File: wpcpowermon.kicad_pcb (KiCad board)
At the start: 2 copper layers, 12 parts, among them J1 Screw_Terminal_01x02, J1001 Conn_02x17_Odd_Even, U3 74HC245, U4 74HC245, U6 MAX485E

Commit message: Version 0.1
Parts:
- added ?: MountingHole_3mm, MountingHole:MountingHole_3mm, F.Cu at (151.4, 66.0)
- added ?: MountingHole_3mm, MountingHole:MountingHole_3mm, F.Cu at (84.8, 123.4)
- added ?: MountingHole_3mm, MountingHole:MountingHole_3mm, F.Cu at (151.4, 123.4)
- added ?: MountingHole_3mm, MountingHole:MountingHole_3mm, F.Cu at (84.8, 66.0)
- added J2: LED, Connector_Molex:Molex_SL_171971-0004_1x04_P2.54mm_Vertical, F.Cu at (143.3, 67.3)
- added J3: LED, Connector_Molex:Molex_SL_171971-0004_1x04_P2.54mm_Vertical, F.Cu at (143.3, 81.8)
- added J4: Screw_Terminal_01x02, TerminalBlock_4Ucon:TerminalBlock_4Ucon_1x02_P3.50mm_Horizontal, F.Cu at (143.9, 103.4)
- added U5: Pico, MCU_RaspberryPi_and_Boards:RPi_Pico_SMD_TH, F.Cu at (121.9, 89.9)
- J1: value Screw_Terminal_01x02 -> Screw_Terminal_01x04; footprint TerminalBlock_4Ucon:TerminalBlock_4Ucon_1x02_P3.50mm_Horizontal -> TerminalBlock_4Ucon:TerminalBlock_4Ucon_1x04_P3.50mm_Horizontal
- moved J1 83.2 mm to (116.7, 122.3)
- moved R2 63.6 mm to (141.7, 99.1), turned to 180 degrees
- moved U6 55.6 mm to (137.4, 112.0)
- moved R1 52.8 mm to (144.3, 124.5), turned to 180 degrees
- moved JP1 37.7 mm to (132.8, 124.5), turned to 90 degrees
- moved C3 32.8 mm to (148.8, 113.0), turned to -90 degrees
- moved D1 24.3 mm to (140.5, 95.0), turned to 180 degrees
- moved C1 0.89 mm to (99.7, 64.5)
- moved U4 0.51 mm to (97.2, 68.1)
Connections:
- C3 pad 1: +3V3 -> +5V
- D1 pad 2: (no net) -> Net-(D1-Pad2)
- J1 pad 1: Net-(J1-Pad1) -> +5V
- J1 pad 2: Net-(J1-Pad2) -> Net-(R1-Pad1)
- J1001 pad 1: (no net) -> unconnected-(J1001-Pad1)
- J1001 pad 2: (no net) -> unconnected-(J1001-Pad2)
- J1001 pad 3: (no net) -> unconnected-(J1001-Pad3)
- J1001 pad 31: (no net) -> unconnected-(J1001-Pad31)
- J1001 pad 32: (no net) -> unconnected-(J1001-Pad32)
- J1001 pad 33: (no net) -> unconnected-(J1001-Pad33)
- J1001 pad 4: (no net) -> unconnected-(J1001-Pad4)
- J1001 pad 5: (no net) -> unconnected-(J1001-Pad5)
- J1001 pad 6: (no net) -> unconnected-(J1001-Pad6)
- JP1 pad 1: Net-(J1-Pad2) -> Net-(JP1-Pad1)
- R1 pad 1: Net-(J1-Pad1) -> Net-(R1-Pad1)
- U3 pad 11: (no net) -> //ZEROCROSS
- U3 pad 12: (no net) -> //LAMP ROW
- U3 pad 13: (no net) -> //LAMP COL
- U3 pad 14: (no net) -> //SOL2
- U3 pad 15: (no net) -> //SOL4
- U3 pad 16: (no net) -> //SOL3
- U3 pad 17: (no net) -> //SOL1
- U3 pad 18: (no net) -> //TRIACS
- U4 pad 11: (no net) -> /D7
- U4 pad 12: (no net) -> /D6
- U4 pad 13: (no net) -> /D5
- U4 pad 14: (no net) -> /D4
- U4 pad 15: (no net) -> /D3
- U4 pad 16: (no net) -> /D2
- U4 pad 17: (no net) -> /D1
- U4 pad 18: (no net) -> /D0
- U6 pad 1: (no net) -> Net-(U5-Pad22)
- U6 pad 4: (no net) -> Net-(U5-Pad21)
- U6 pad 5: (no net) -> GND
- U6 pad 6: Net-(J1-Pad1) -> Net-(R1-Pad1)
- U6 pad 7: Net-(J1-Pad2) -> Net-(JP1-Pad1)
- U6 pad 8: (no net) -> +5V
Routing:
- net +5V: track 0.00 -> 118.7 mm
- net Net-(R1-Pad1): track 0.00 -> 34.3 mm
- net Net-(JP1-Pad1): track 0.00 -> 28.4 mm
- net Net-(J2-Pad3): track 0.00 -> 23.1 mm
- net Net-(J3-Pad3): track 0.00 -> 21.9 mm
- net Net-(J3-Pad2): track 0.00 -> 21.6 mm
- net Net-(J2-Pad2): track 0.00 -> 20.3 mm
- net //SOL3: track 0.00 -> 17.8 mm
- net //SOL4: track 0.00 -> 17.3 mm
- net //SOL2: track 0.00 -> 17.0 mm
- net //SOL1: track 0.00 -> 17.0 mm
- net //TRIACS: track 0.00 -> 16.8 mm
- net Net-(U5-Pad24): track 0.00 -> 15.3 mm
- net //LAMP COL: track 0.00 -> 14.5 mm
- net //LAMP ROW: track 0.00 -> 14.3 mm
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- added copper zone on F.Cu, net +3V3
- added copper zone on B.Cu, net GND
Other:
- board outline added: 75.2 x 66.5 mm
- board text added: "+ A B -"
- board text added: "1"
- board text added: "TERM"
- board text added: "WPC PowerMON 0.1 (c) 2021 pinball-power.com"

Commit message: v 0.2
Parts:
- removed ? (x4): MountingHole_3mm, MountingHole:MountingHole_3mm
- removed J2: LED, Connector_Molex:Molex_SL_171971-0004_1x04_P2.54mm_Vertical
- removed U6: MAX485E, Package_DIP:DIP-8_W7.62mm_LongPads
- added J10: IO5, Connector_Molex:Molex_KK-254_AE-6410-03A_1x03_P2.54mm_Vertical, F.Cu at (154.3, 102.2)
- added J11: IO7, Connector_Molex:Molex_KK-254_AE-6410-03A_1x03_P2.54mm_Vertical, F.Cu at (154.3, 118.7)
- added J12: RS485, TerminalBlock_4Ucon:TerminalBlock_4Ucon_1x04_P3.50mm_Horizontal, F.Cu at (163.6, 81.9)
- added J5: IO4+3, Connector_Molex:Molex_KK-254_AE-6410-04A_1x04_P2.54mm_Vertical, F.Cu at (144.2, 88.3)
- added J6: IO6+5, Connector_Molex:Molex_KK-254_AE-6410-04A_1x04_P2.54mm_Vertical, F.Cu at (144.2, 104.8)
- added J7: IO8+7, Connector_Molex:Molex_KK-254_AE-6410-04A_1x04_P2.54mm_Vertical, F.Cu at (144.2, 121.3)
- added J8: IO1, Connector_Molex:Molex_KK-254_AE-6410-03A_1x03_P2.54mm_Vertical, F.Cu at (154.3, 69.2)
- added J9: IO3, Connector_Molex:Molex_KK-254_AE-6410-03A_1x03_P2.54mm_Vertical, F.Cu at (154.3, 85.7)
- added JP2: 5V, Connector_PinHeader_2.54mm:PinHeader_1x02_P2.54mm_Vertical, F.Cu at (155.6, 123.2)
- added JP3: 5V, Connector_PinHeader_2.54mm:PinHeader_1x02_P2.54mm_Vertical, F.Cu at (142.9, 125.7)
- added JP4: 5V, Connector_PinHeader_2.54mm:PinHeader_1x02_P2.54mm_Vertical, F.Cu at (155.6, 106.7)
- added JP5: 5V, Connector_PinHeader_2.54mm:PinHeader_1x02_P2.54mm_Vertical, F.Cu at (142.9, 109.2)
- added JP6: 5V, Connector_PinHeader_2.54mm:PinHeader_1x02_P2.54mm_Vertical, F.Cu at (154.9, 90.2)
- added JP7: 5V, Connector_PinHeader_2.54mm:PinHeader_1x02_P2.54mm_Vertical, F.Cu at (142.9, 92.7)
- added JP8: 5V, Connector_PinHeader_2.54mm:PinHeader_1x02_P2.54mm_Vertical, F.Cu at (155.6, 73.7)
- added JP9: 5V, Connector_PinHeader_2.54mm:PinHeader_1x02_P2.54mm_Vertical, F.Cu at (142.9, 76.2)
- added REF**: MountingHole_4.3mm_M4, MountingHole:MountingHole_4.3mm_M4, F.Cu at (84.8, 66.0)
- added REF**: MountingHole_4.3mm_M4, MountingHole:MountingHole_4.3mm_M4, F.Cu at (174.2, 66.0)
- added REF**: MountingHole_4.3mm_M4, MountingHole:MountingHole_4.3mm_M4, F.Cu at (174.2, 123.4)
- added REF**: MountingHole_4.3mm_M4, MountingHole:MountingHole_4.3mm_M4, F.Cu at (84.8, 123.4)
- added REF**: OSHW-Logo2_14.6x12mm_SilkScreen, Symbol:OSHW-Logo2_14.6x12mm_SilkScreen, F.Cu at (122.2, 104.4)
- added U1: MAX485E, Package_DIP:DIP-8_W7.62mm_LongPads, F.Cu at (163.8, 94.3)
- J1: value Screw_Terminal_01x04 -> RS232; footprint TerminalBlock_4Ucon:TerminalBlock_4Ucon_1x04_P3.50mm_Horizontal -> Connector_Molex:Molex_KK-254_AE-6410-04A_1x04_P2.54mm_Vertical
- J1001: value Conn_02x17_Odd_Even -> WPC Bus
- J3: value LED -> IO2+1; footprint Connector_Molex:Molex_SL_171971-0004_1x04_P2.54mm_Vertical -> Connector_Molex:Molex_KK-254_AE-6410-04A_1x04_P2.54mm_Vertical
- J4: value Screw_Terminal_01x02 -> 5V
- JP1: value Jumper -> TERM
- moved J1 56.2 mm to (171.4, 109.5), turned to 180 degrees
- moved R1 55.1 mm to (170.4, 75.9), turned to 0 degrees
- moved JP1 52.1 mm to (170.9, 88.9)
- moved J4 31.6 mm to (118.7, 122.6), turned to 180 degrees
- moved C3 31.0 mm to (175.2, 96.8)
- moved R2 30.9 mm to (125.1, 125.1), turned to 0 degrees
- moved D1 28.7 mm to (127.6, 120.7)
- moved J3 10.1 mm to (144.2, 71.8), turned to 90 degrees
- moved J1001 1.55 mm to (86.1, 115.3)
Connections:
- D1 pad 2: Net-(D1-Pad2) -> +5V
- J1 pad 1: +5V -> GND
- J1 pad 2: Net-(R1-Pad1) -> /io/TX
- J1 pad 3: Net-(JP1-Pad1) -> /io/RX
- J1 pad 4: GND -> +5V
- J3 pad 1: +5V -> GND
- J3 pad 2: Net-(J3-Pad2) -> /io/IO2
- J3 pad 4: GND -> /io/IO1
- JP1 pad 1: Net-(JP1-Pad1) -> Net-(J12-Pad3)
- R1 pad 1: Net-(R1-Pad1) -> Net-(J12-Pad2)
- U5 pad 21: Net-(U5-Pad21) -> /io/TX
- U5 pad 22: Net-(U5-Pad22) -> /io/RX
- U5 pad 24: Net-(U5-Pad24) -> /io/IO8
- U5 pad 25: Net-(D1-Pad2) -> /io/IO7
- U5 pad 26: Net-(J3-Pad3) -> /io/IO6
- U5 pad 27: Net-(J3-Pad2) -> /io/IO5
- U5 pad 29: unconnected-(U5-Pad29) -> /io/IO4
- U5 pad 31: unconnected-(U5-Pad31) -> /io/IO3
- U5 pad 32: Net-(J2-Pad3) -> /io/IO2
- U5 pad 34: Net-(J2-Pad2) -> /io/IO1
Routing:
- net +5V: track 118.7 -> 197.6 mm
- net /io/TX: track 0.00 -> 60.8 mm
- net /io/RX: track 0.00 -> 59.7 mm
- net /io/IO8: track 0.00 -> 55.8 mm
- net +3V3: track 11.2 -> 64.9 mm
- net /io/IO1: track 0.00 -> 37.2 mm
- net Net-(R1-Pad1): track 34.3 -> 0.00 mm
- net /io/IO3: track 0.00 -> 30.0 mm
- net /io/IO7: track 0.00 -> 28.6 mm
- net Net-(JP1-Pad1): track 28.4 -> 0.00 mm
- net /io/IO2: track 0.00 -> 27.9 mm
- net Net-(J12-Pad2): track 0.00 -> 26.5 mm
- net /io/IO5: track 0.00 -> 25.3 mm
- net Net-(J2-Pad3): track 23.1 -> 0.00 mm
- net Net-(J3-Pad2): track 21.6 -> 0.00 mm
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- added copper zone on F.Cu, net +5V
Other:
- board size 75.2 x 66.5 mm -> 98.6 x 66.6 mm
- board text added: "WPC PowerMON v 0.2 (c) 2021 pinball-power.com"
- board text removed: "+ A B -"
- board text removed: "TERM"
- board text removed: "WPC PowerMON 0.1 (c) 2021 pinball-power.com"

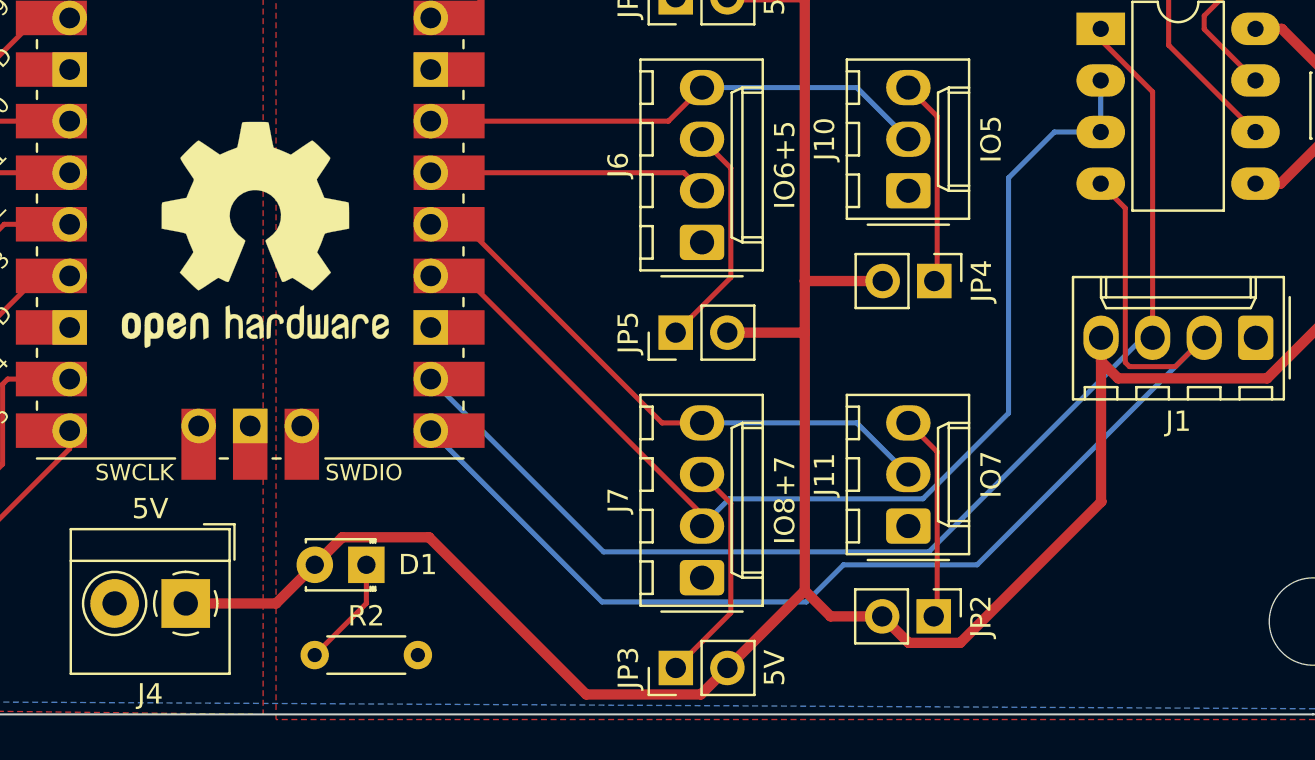
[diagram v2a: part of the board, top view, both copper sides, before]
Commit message: Added OHC logo
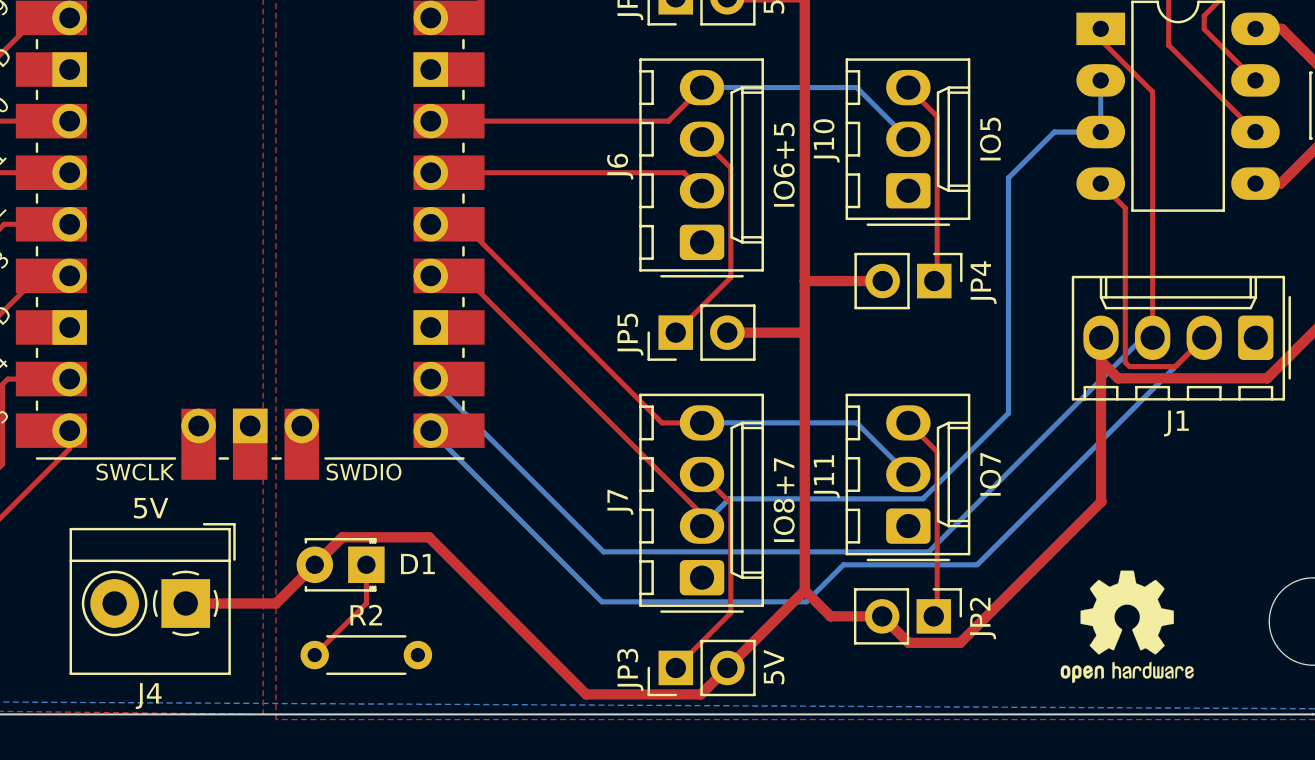
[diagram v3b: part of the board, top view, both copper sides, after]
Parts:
- removed the REF** at (122.2, 104.4)
- added REF**: OSHW-Logo2_7.3x6mm_SilkScreen, Symbol:OSHW-Logo2_7.3x6mm_SilkScreen, F.Cu at (165.1, 123.7)
